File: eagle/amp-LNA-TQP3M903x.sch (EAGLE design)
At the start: 20 parts, among them J1 142-0701-851, J2 142-0701-851, U1 TQP3M9036

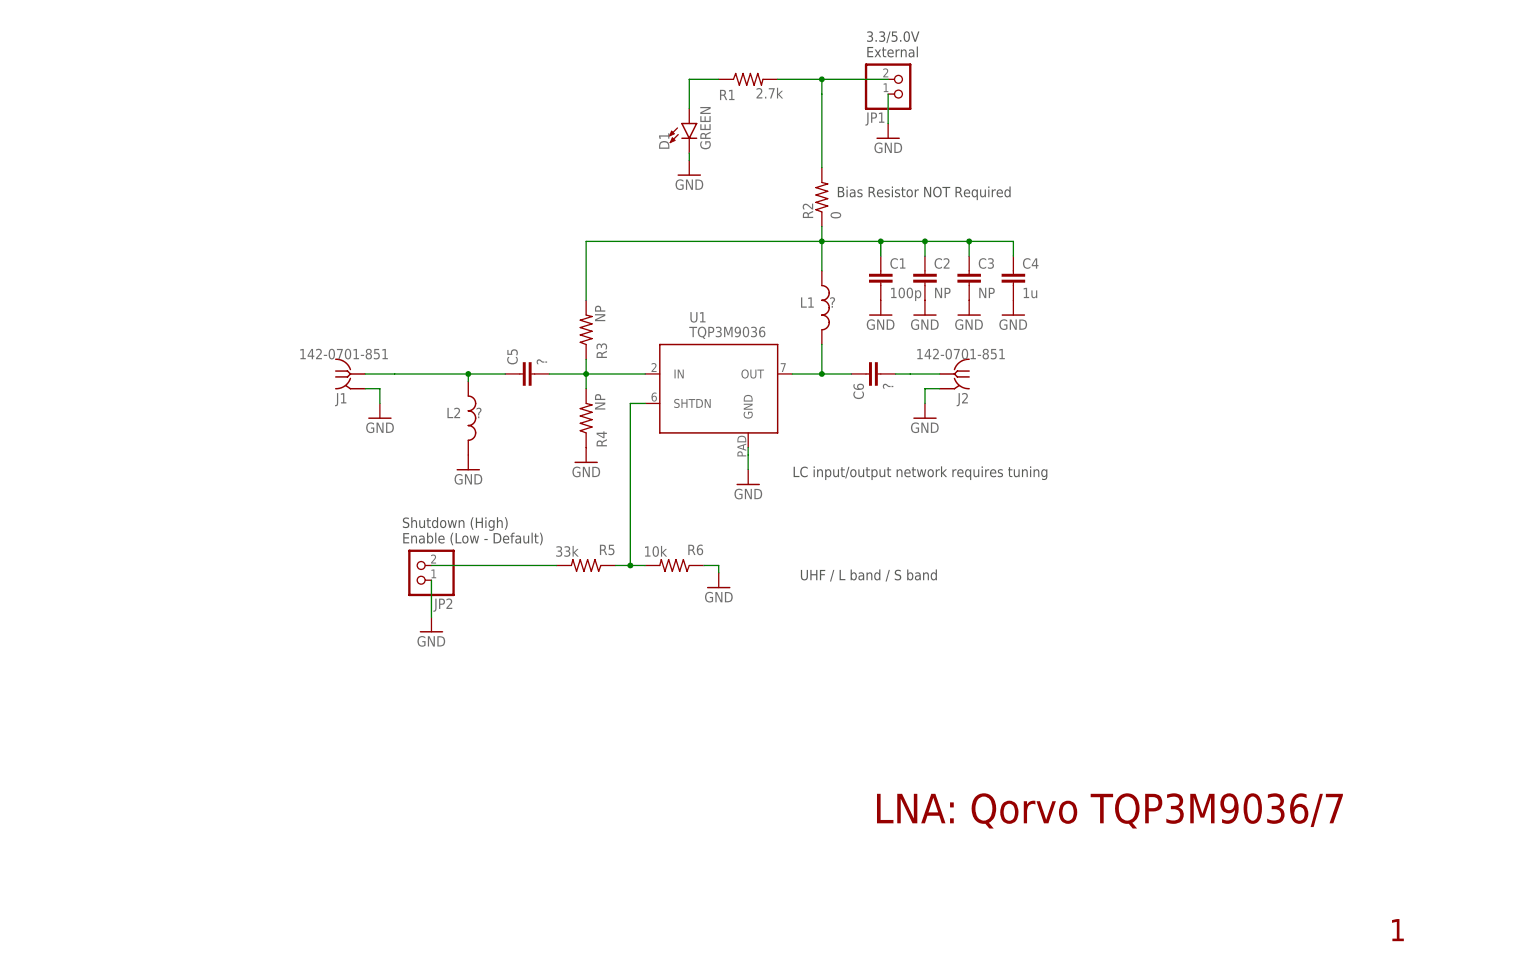
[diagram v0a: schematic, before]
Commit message: Update passives' footprint
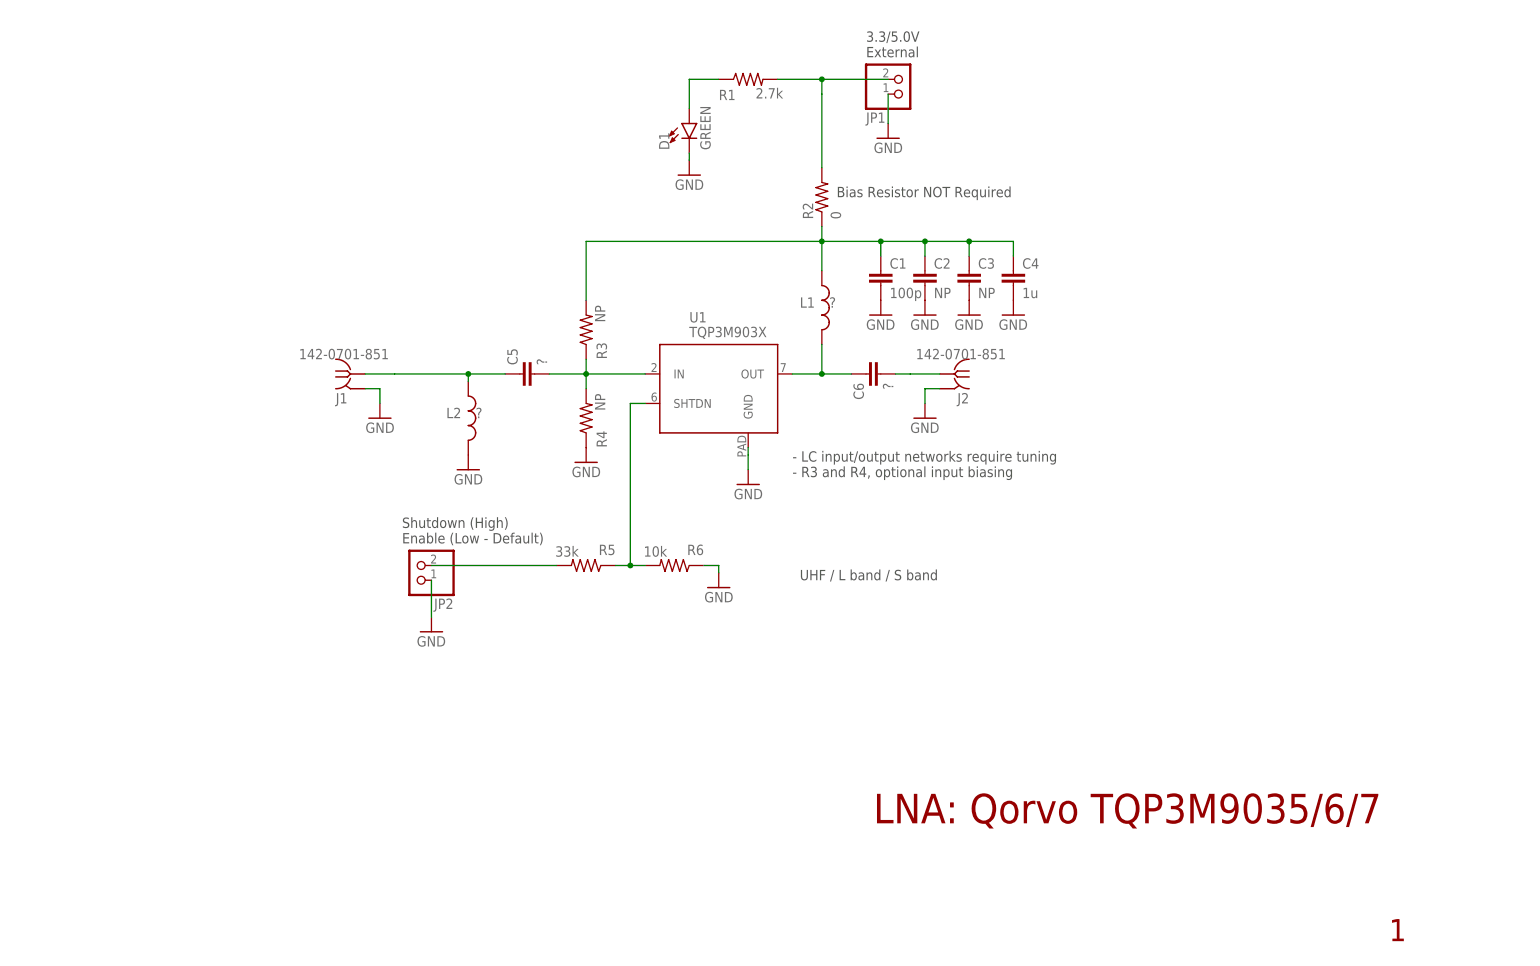
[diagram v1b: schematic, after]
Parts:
- C5, C6: device oresat-rcl:C-EU0402-B-NOSILK -> oresat-rcl:C-EU0402-C-NOSILK
- L1: device oresat-rcl:L-US0603-B-NOSILK -> oresat-rcl:L-US0603-C-NOSILK
- L2: device oresat-rcl:L-US0402-B-NOSILK -> oresat-rcl:L-US0402-C-NOSILK
- R3, R4: device oresat-rcl:R-US_0402-B-NOSILK -> oresat-rcl:R-US_0402-C-NOSILK
- U1: value TQP3M9036 -> TQP3M903X; device U-Qorvo-TQP3M9036-LNA:TQP3M9036 -> U-Qorvo-TQP3M903x-LNA:TQP3M903X
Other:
- note added: "- LC input/output networks require tuning - R3 and R4, optional input biasing"
- note added: "LNA: Qorvo TQP3M9035/6/7"
- note removed: "LC input/output network requires tuning"
- note removed: "LNA: Qorvo TQP3M9036/7"
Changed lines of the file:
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@@
 <class number="0" name="default" width="0" drill="0">
+</class>
+<class number="1" name="RF1" width="0" drill="0">
+<clearance class="1" value="0.5"/>
+</class>
+<class number="2" name="RF2" width="0" drill="0">
+<clearance class="2" value="0.8"/>
 </class>
 </classes>
 <parts>
 <part name="FRAME2" library="frames" library_urn="urn:adsk.eagle:library:229" deviceset="FRAME_A_L" device=""/>
-<part name="U1" library="U-Qorvo-TQP3M9036-LNA" deviceset="TQP3M9036" device=""/>
+<part name="U1" library="U-Qorvo-TQP3M903x-LNA" deviceset="TQP3M903X" device=""/>
 <part name="GND26" library="supply1" library_urn="urn:adsk.eagle:library:371" deviceset="GND" device=""/>
 <part name="C1" library="oresat-rcl" deviceset="C-EU" device="0603-B-NOSILK" value="100p"/>
 <part name="GND27" library="supply1" library_urn="urn:adsk.eagle:library:371" deviceset="GND" device=""/>
 <part name="GND28" library="supply1" library_urn="urn:adsk.eagle:library:371" deviceset="GND" device=""/>
-<part name="C6" library="oresat-rcl" deviceset="C-EU" device="0402-B-NOSILK" value="?"/>
-<part name="C5" library="oresat-rcl" deviceset="C-EU" device="0402-B-NOSILK" value="?"/>
+<part name="C6" library="oresat-rcl" deviceset="C-EU" device="0402-C-NOSILK" value="?"/>
+<part name="C5" library="oresat-rcl" deviceset="C-EU" device="0402-C-NOSILK" value="?"/>
 <part name="GND29" library="supply1" library_urn="urn:adsk.eagle:library:371" deviceset="GND" device=""/>
 <part name="GND30" library="supply1" library_urn="urn:adsk.eagle:library:371" deviceset="GND" device=""/>
@@
 <part name="J1" library="J-Cinch-142-0701-851-SMA-end-launch" deviceset="142-0701-851" device=""/>
 <part name="J2" library="J-Cinch-142-0701-851-SMA-end-launch" deviceset="142-0701-851" device=""/>
-<part name="R3" library="oresat-rcl" deviceset="R-US_" device="0402-B-NOSILK" value="NP"/>
-<part name="R4" library="oresat-rcl" deviceset="R-US_" device="0402-B-NOSILK" value="NP"/>
+<part name="R3" library="oresat-rcl" deviceset="R-US_" device="0402-C-NOSILK" value="NP"/>
+<part name="R4" library="oresat-rcl" deviceset="R-US_" device="0402-C-NOSILK" value="NP"/>
 <part name="GND2" library="supply1" library_urn="urn:adsk.eagle:library:371" deviceset="GND" device=""/>
 <part name="R5" library="oresat-rcl" deviceset="R-US_" device="0603-B-NOSILK" value="33k"/>
 <part name="R6" library="oresat-rcl" deviceset="R-US_" device="0603-B-NOSILK" value="10k"/>
 <part name="GND3" library="supply1" library_urn="urn:adsk.eagle:library:371" deviceset="GND" device=""/>
-<part name="L2" library="oresat-rcl" deviceset="L-US" device="0402-B-NOSILK" value="?"/>
+<part name="L2" library="oresat-rcl" deviceset="L-US" device="0402-C-NOSILK" value="?"/>
 <part name="GND5" library="supply1" library_urn="urn:adsk.eagle:library:371" deviceset="GND" device=""/>
-<part name="L1" library="oresat-rcl" deviceset="L-US" device="0603-B-NOSILK" value="?"/>
+<part name="L1" library="oresat-rcl" deviceset="L-US" device="0603-C-NOSILK" value="?"/>
 </parts>
 <sheets>
 <sheet>
 <plain>
-<text x="176.53" y="26.67" size="5.08" layer="94">LNA: Qorvo TQP3M9036/7</text>
+<text x="176.53" y="26.67" size="5.08" layer="94">LNA: Qorvo TQP3M9035/6/7</text>
 <text x="265.43" y="6.35" size="3.81" layer="94">1</text>
-<text x="162.56" y="86.36" size="1.778" layer="97">LC input/output network requires tuning</text>
+<text x="162.56" y="86.36" size="1.778" layer="97">- LC input/output networks require tuning
+- R3 and R4, optional input biasing</text>
 <text x="170.18" y="134.62" size="1.778" layer="97">Bias Resistor NOT Required</text>
 <text x="163.83" y="68.58" size="1.778" layer="97">UHF / L band / S band</text>
@@
 </segment>
 </net>
-<net name="N$28" class="0">
+<net name="N$28" class="1">
 <segment>
 <pinref part="U1" gate="G$1" pin="OUT"/>
@@
 </segment>
 </net>
-<net name="N$32" class="0">
+<net name="N$32" class="1">
 <segment>
 <pinref part="C5" gate="CE" pin="2"/>
@@
 </segment>
 </net>
-<net name="N$34" class="0">
+<net name="N$34" class="2">
 <segment>
 <wire x1="182.88" y1="104.14" x2="187.96" y2="104.14" width="0.1524" layer="91"/>
@@
 </segment>
 </net>
-<net name="N$39" class="0">
+<net name="N$39" class="2">
 <segment>
 <wire x1="93.98" y1="104.14" x2="88.9" y2="104.14" width="0.1524" layer="91"/>

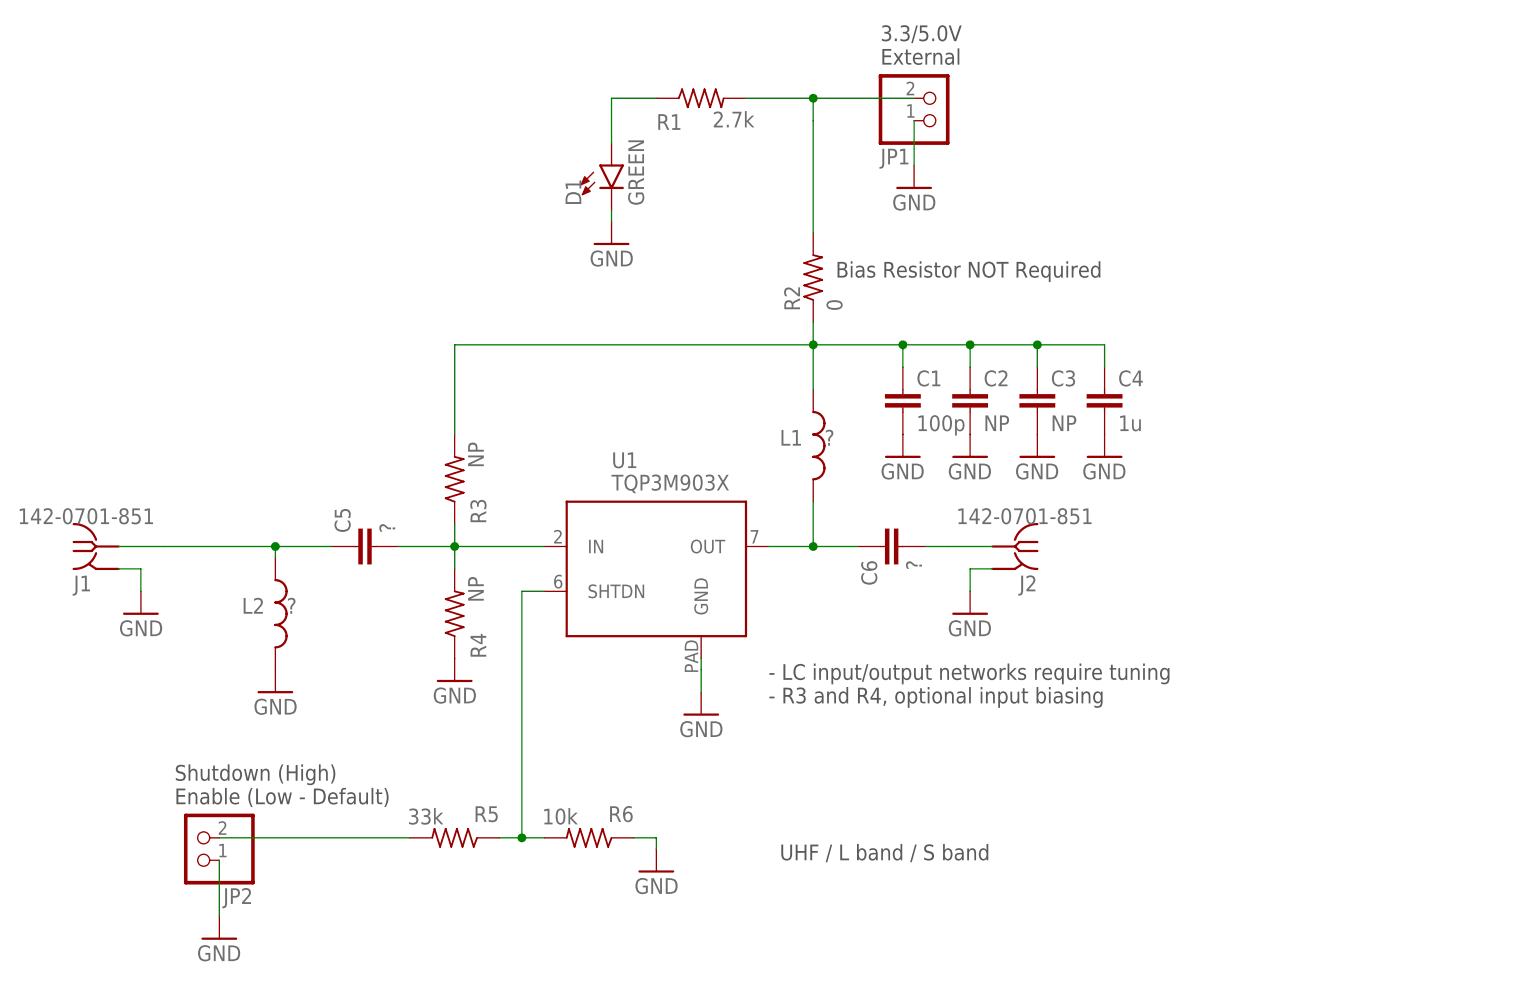
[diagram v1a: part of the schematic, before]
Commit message: Completed TQP3M903x layout
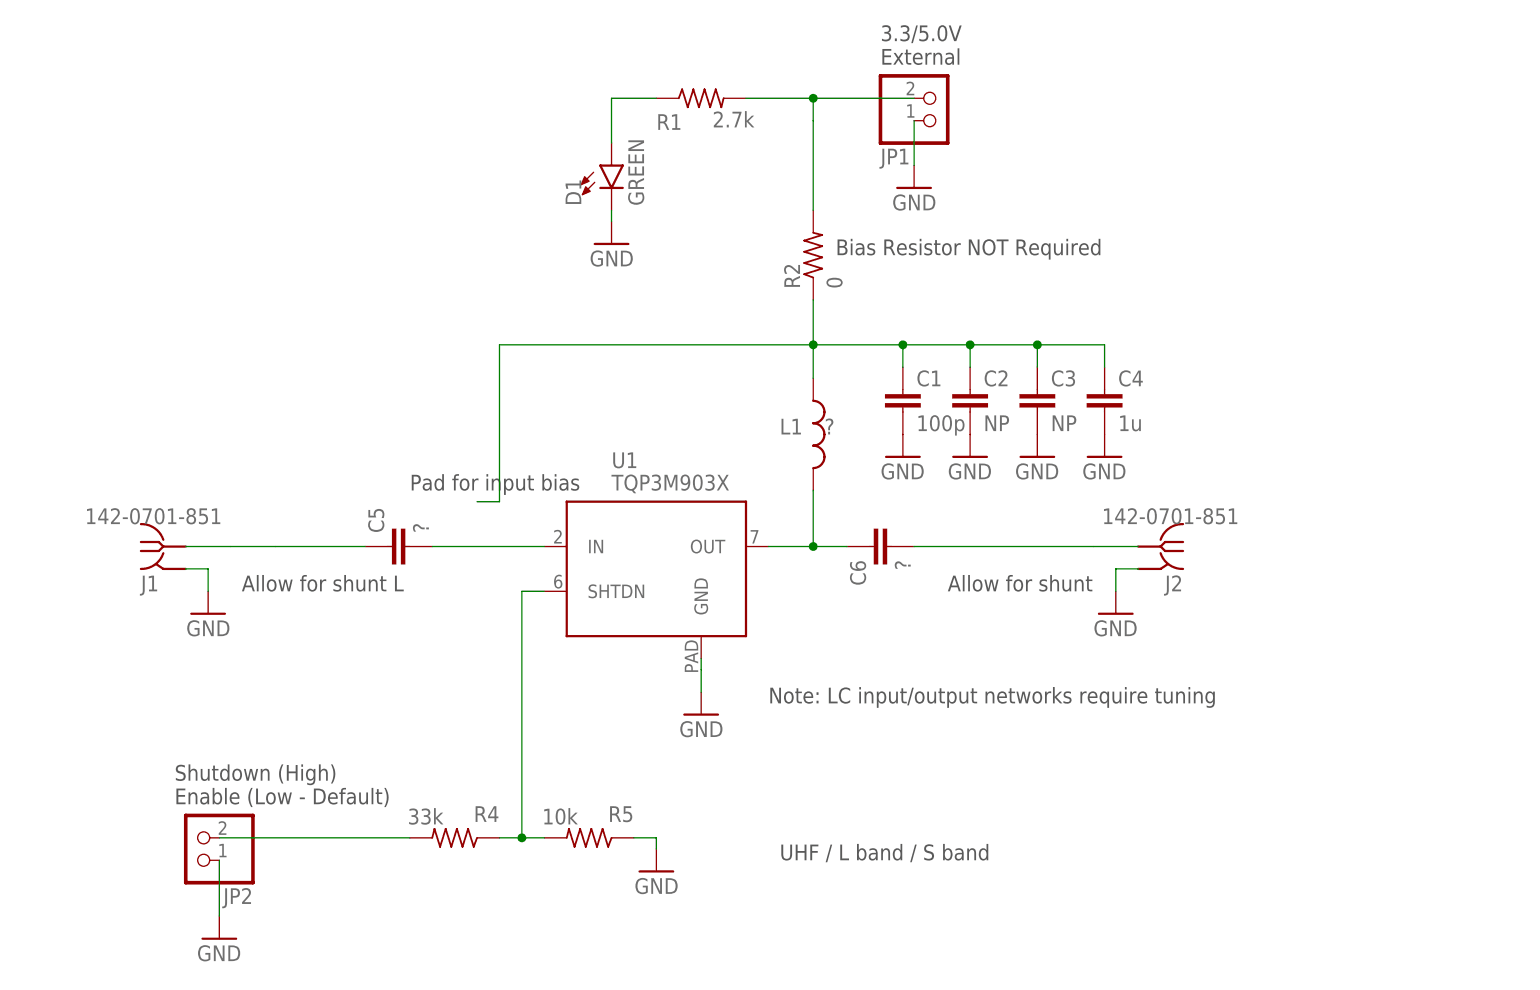
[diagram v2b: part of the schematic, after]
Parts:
- removed L2: ?, oresat-rcl:L-US0402-C-NOSILK
- removed R3: NP, oresat-rcl:R-US_0402-C-NOSILK
- removed R6: 10k, oresat-rcl:R-US_0603-B-NOSILK
- R4: value NP -> 33k; device oresat-rcl:R-US_0402-C-NOSILK -> oresat-rcl:R-US_0603-B-NOSILK
- R5: value 33k -> 10k
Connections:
- net N$34 renamed RF_OUT
- removed net N$39: C5.1, J1.RF, L2.1
- new net RF_IN: C5.1, J1.RF
- net GND: now also R5.1; no longer L2.2, R4.1, R6.1
- net N$2: now also R4.1, R5.2; no longer R5.1, R6.2
- net N$3: now also R4.2; no longer R5.2
- net N$32: no longer R3.1, R4.2
- net N$47: no longer R3.2
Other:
- note added: "Allow for shunt"
- note added: "Allow for shunt L"
- note added: "Note: LC input/output networks require tuning"
- note added: "Pad for input bias"
- note removed: "- LC input/output networks require tuning - R3 and R4, optional input biasing"
- moved on the sheet: C5, C6, J1, J2, L1, R2, R4, R5
